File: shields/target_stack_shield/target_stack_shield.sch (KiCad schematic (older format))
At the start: 12 parts, among them IC1 NCP1117DT33T5G, J1 GPIO shield connector 40pin, J2 probe shield connector 26pin, J3 PCIE-064-02-X-D-RA

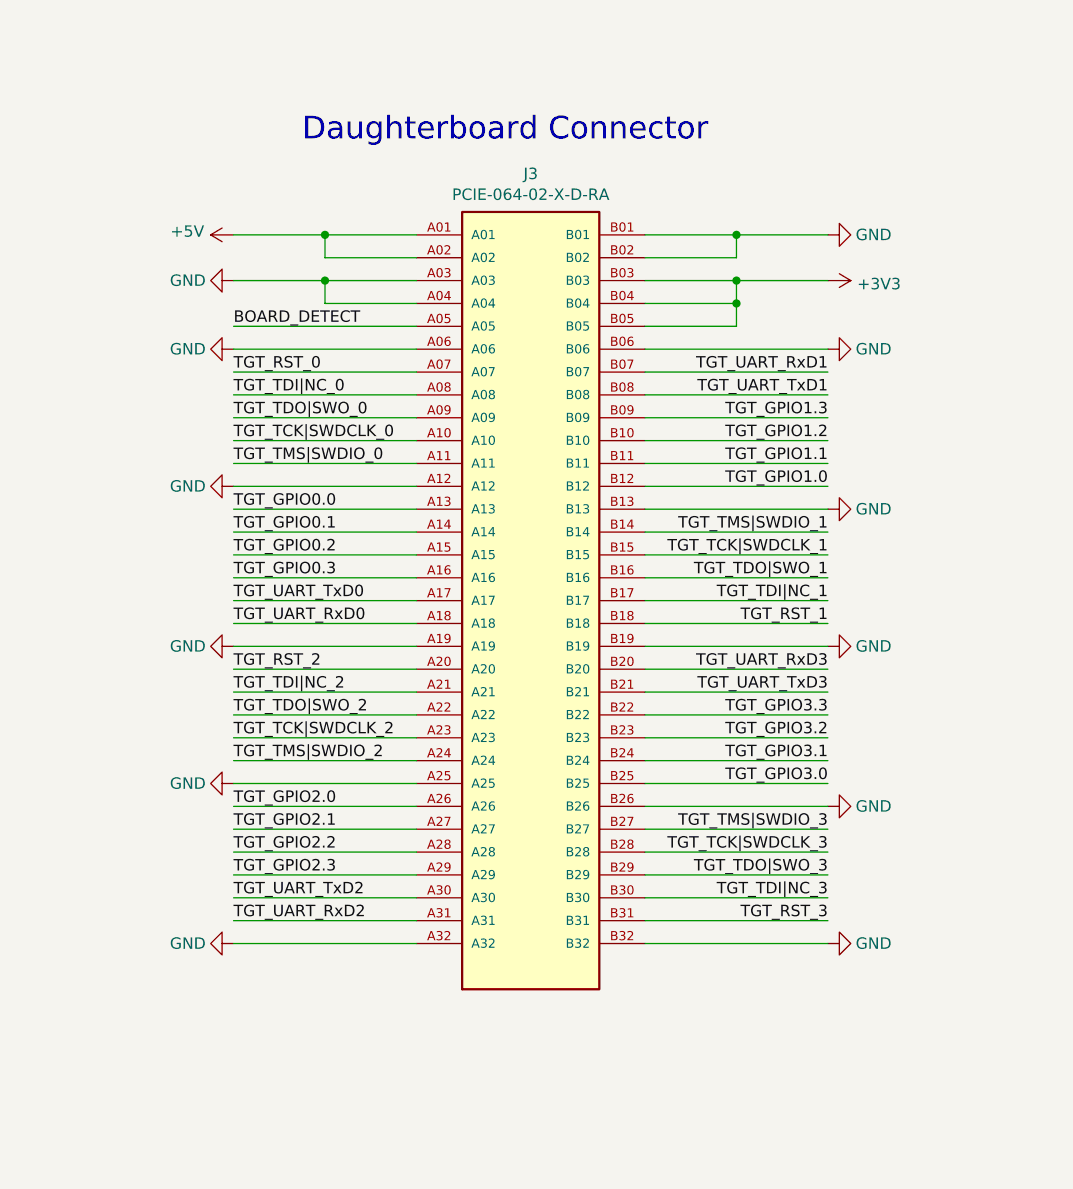
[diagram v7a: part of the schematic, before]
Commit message: changed PCIE 64 to M.2 Key B connector
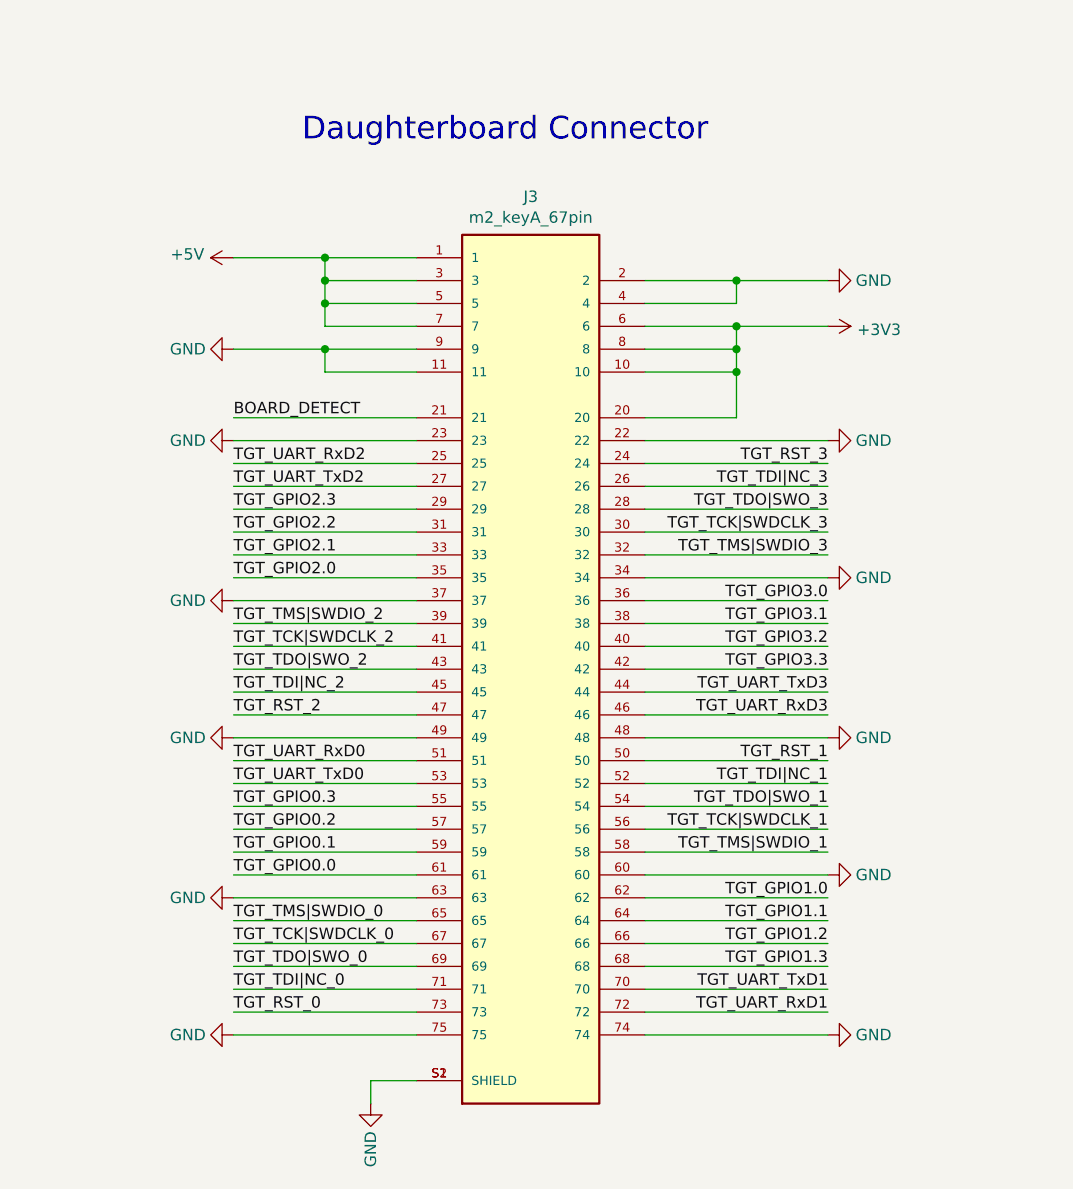
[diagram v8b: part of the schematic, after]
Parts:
- removed J3: PCIE-064-02-X-D-RA, hive:SAMTEC_PCIE-064-02-X-D-RA, symbol hive:PCIE-064-02-X-D-RA
- added J3: m2_keyA_67pin, hive:TE_2199230-3, symbol hive:m2_keyA_67pin
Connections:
- net +3V3: now also J3.10, J3.20, J3.6, J3.8
- net +5V: now also J3.1, J3.3, J3.5, J3.7
- net BOARD_DETECT: now also J3.21
- net GND: now also J3.11, J3.2, J3.22, J3.23, J3.34, J3.37, J3.4, J3.48, J3.49, J3.60, J3.63, J3.74, J3.75, J3.9, J3.S1 (SHIELD), J3.S2 (SHIELD)
- net TGT_GPIO0.0: now also J3.61
- net TGT_GPIO0.1: now also J3.59
- net TGT_GPIO0.2: now also J3.57
- net TGT_GPIO0.3: now also J3.55
- net TGT_GPIO1.0: now also J3.62
- net TGT_GPIO1.1: now also J3.64
- net TGT_GPIO1.2: now also J3.66
- net TGT_GPIO1.3: now also J3.68
- net TGT_GPIO2.0: now also J3.35
- net TGT_GPIO2.1: now also J3.33
- net TGT_GPIO2.2: now also J3.31
- net TGT_GPIO2.3: now also J3.29
- net TGT_GPIO3.0: now also J3.36
- net TGT_GPIO3.1: now also J3.38
- net TGT_GPIO3.2: now also J3.40
- net TGT_GPIO3.3: now also J3.42
- net TGT_RST_0: now also J3.73
- net TGT_RST_1: now also J3.50
- net TGT_RST_2: now also J3.47
- net TGT_RST_3: now also J3.24
- net TGT_TCK|SWDCLK_0: now also J3.67
- net TGT_TCK|SWDCLK_1: now also J3.56
- net TGT_TCK|SWDCLK_2: now also J3.41
- net TGT_TCK|SWDCLK_3: now also J3.30
- net TGT_TDI|NC_0: now also J3.71
- net TGT_TDI|NC_1: now also J3.52
- net TGT_TDI|NC_2: now also J3.45
- net TGT_TDI|NC_3: now also J3.26
- net TGT_TDO|SWO_0: now also J3.69
- net TGT_TDO|SWO_1: now also J3.54
- net TGT_TDO|SWO_2: now also J3.43
- net TGT_TDO|SWO_3: now also J3.28
- net TGT_TMS|SWDIO_0: now also J3.65
- net TGT_TMS|SWDIO_1: now also J3.58
- net TGT_TMS|SWDIO_2: now also J3.39
- net TGT_TMS|SWDIO_3: now also J3.32
- net TGT_UART_RxD0: now also J3.51
- net TGT_UART_RxD1: now also J3.72
- net TGT_UART_RxD2: now also J3.25
- net TGT_UART_RxD3: now also J3.46
- net TGT_UART_TxD0: now also J3.53
- net TGT_UART_TxD1: now also J3.70
- net TGT_UART_TxD2: now also J3.27
- net TGT_UART_TxD3: now also J3.44
